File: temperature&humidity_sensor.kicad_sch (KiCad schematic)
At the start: 6 parts, among them U35 HDC1080

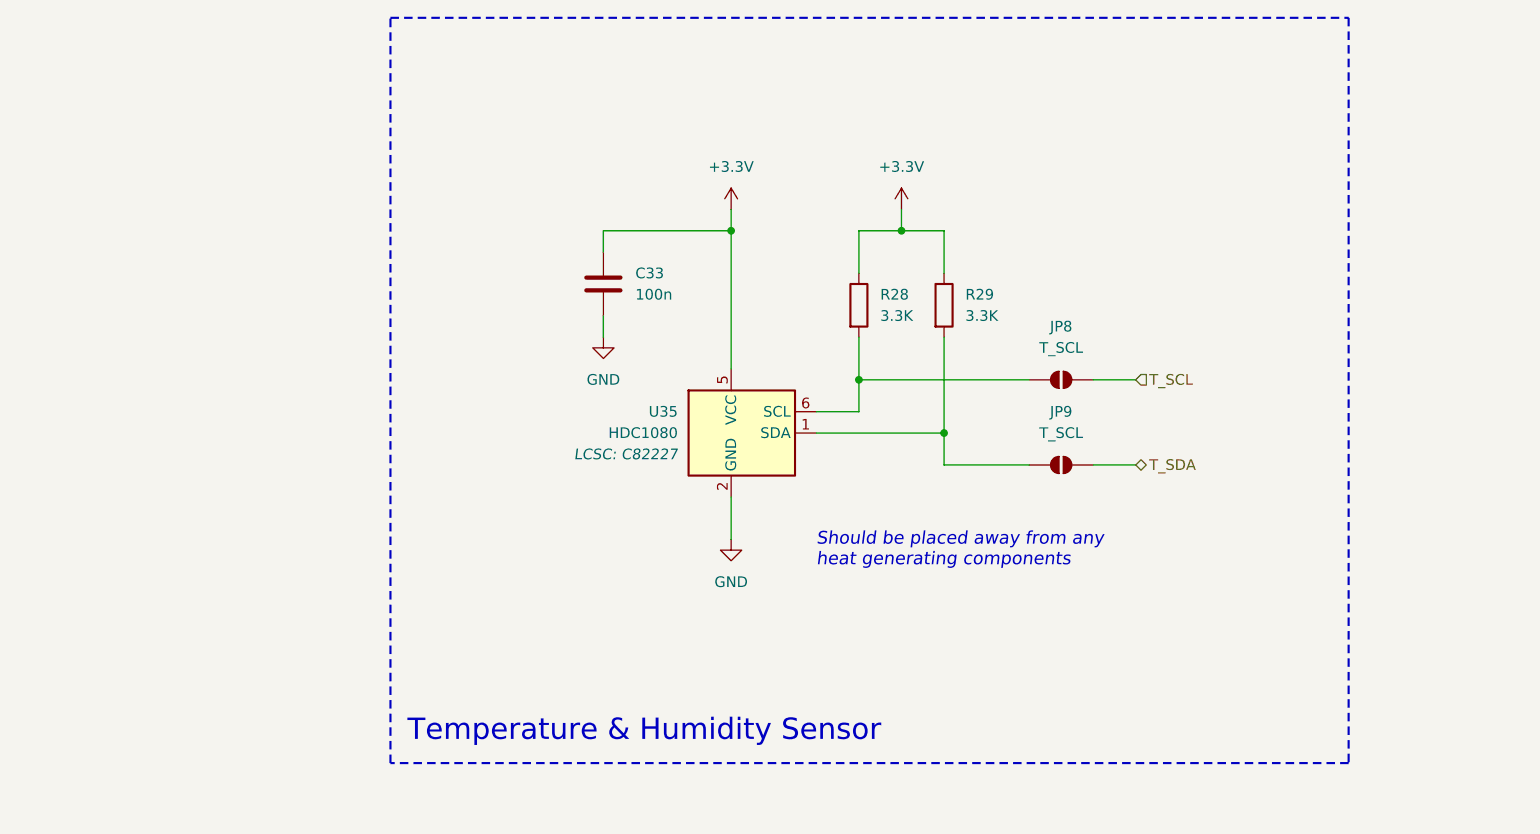
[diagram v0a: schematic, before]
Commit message: addition of bus
- cleaned up the structure of the schematic.
- addition of the colon
- root schematic improvements
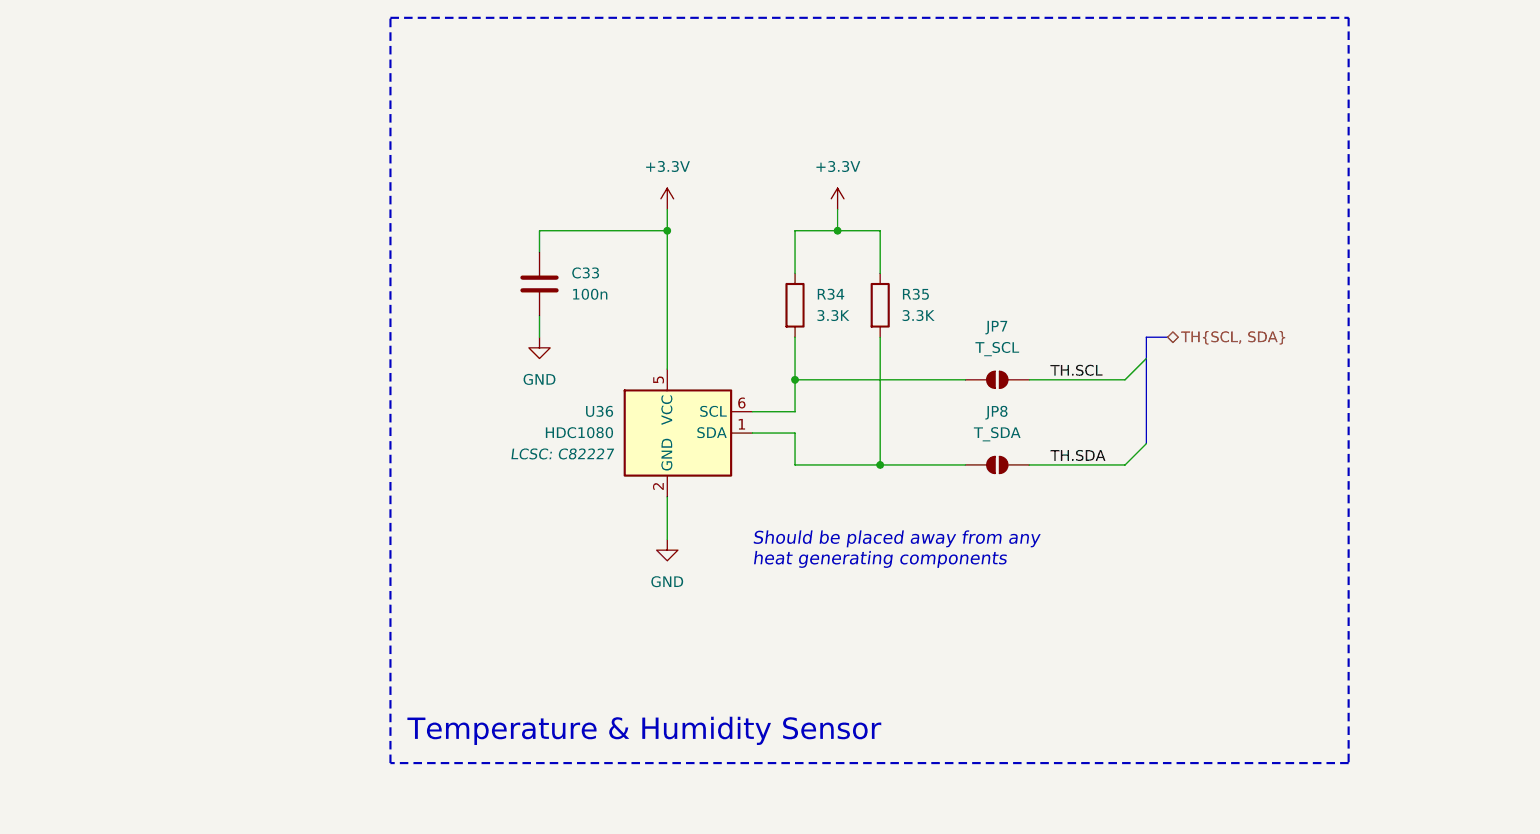
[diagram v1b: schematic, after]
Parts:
- JP8: renamed from JP9; value T_SCL -> T_SDA
- renumbered JP8 to JP7, R28 to R34, R29 to R35, U35 to U36
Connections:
- net T_SCL renamed TH.SCL
- net T_SDA renamed TH.SDA
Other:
- moved on the sheet: C33, JP7, JP8, R34, R35, U36

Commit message: current limiting resistor changes
- added colon led model, but might replace it in the future.
- reduction in current limiting resistance.
- removed the solder jumps in the individual circuit schematics.
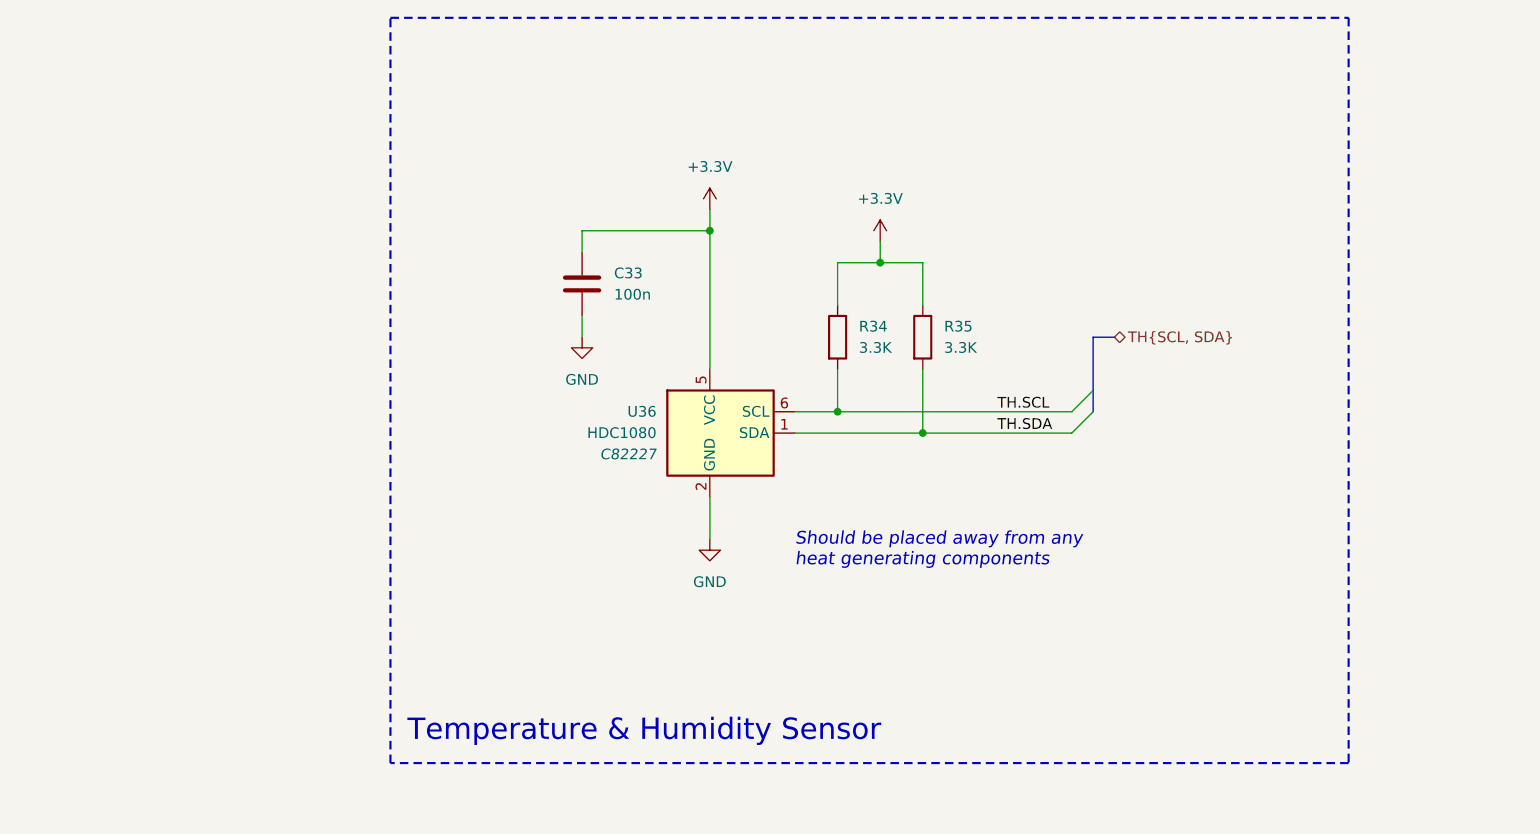
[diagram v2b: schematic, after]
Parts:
- removed JP7: T_SCL, Jumper:SolderJumper-2_P1.3mm_Open_TrianglePad1.0x1.5mm, symbol Jumper:SolderJumper_2_Open
- removed JP8: T_SDA, Jumper:SolderJumper-2_P1.3mm_Open_TrianglePad1.0x1.5mm, symbol Jumper:SolderJumper_2_Open
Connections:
- net TH.SCL: now also R34.2, U36.6 (SCL)
- net TH.SDA: now also R35.2, U36.1 (SDA)
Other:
- moved on the sheet: C33, R34, R35, U36

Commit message: voltage regulation changes
- ambient light sensor addition
- colon control
- brightness control through regulators
- added test points
- MCU pinout changes
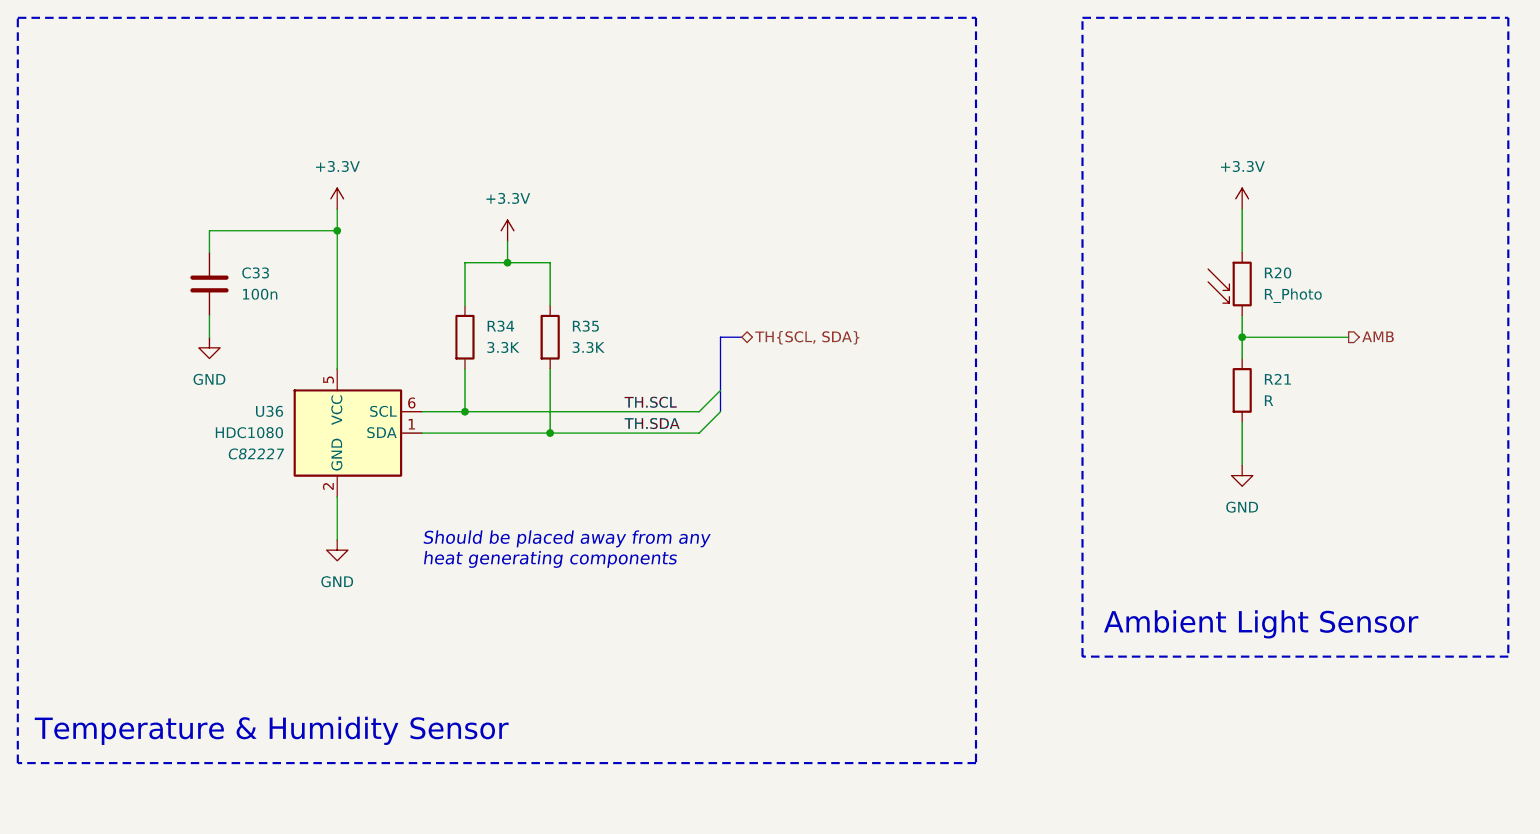
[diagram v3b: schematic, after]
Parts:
- added R20: R_Photo, symbol Device:R_Photo
- added R21: R, symbol Device:R
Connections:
- net +3.3V: now also R20.1
- net GND: now also R21.2
- new net AMB: R20.2, R21.1
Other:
- note added: "Ambient Light Sensor"
- moved on the sheet: C33, R34, R35, U36

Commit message: buzzer addition
- reordering
- test point addition
- ferrite beads on both the MCUs
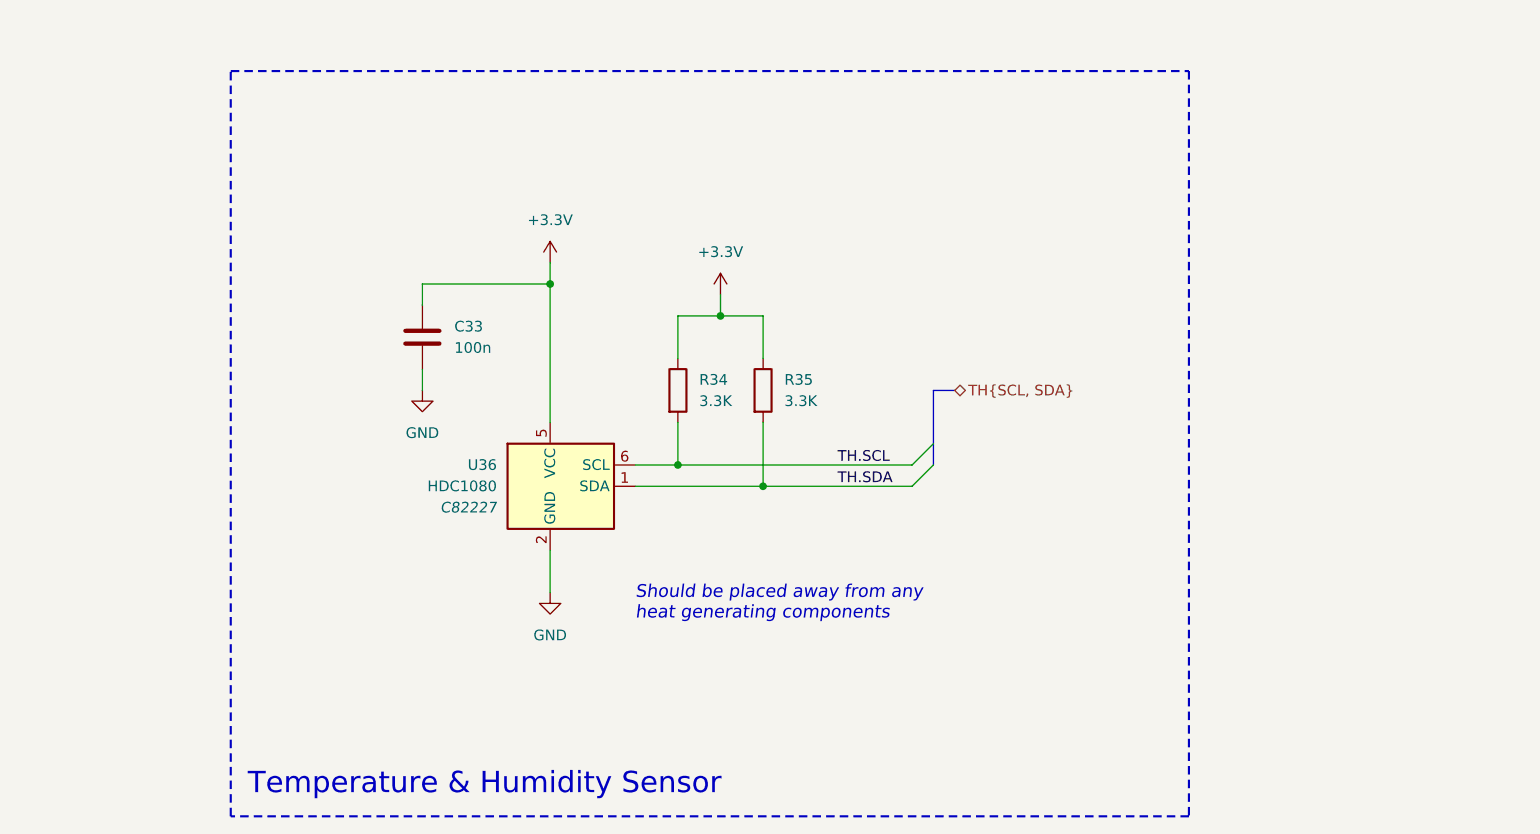
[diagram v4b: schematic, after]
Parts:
- removed R20: R_Photo, symbol Device:R_Photo
- removed R21: R, symbol Device:R
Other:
- note removed: "Ambient Light Sensor"
- moved on the sheet: C33, R34, R35, U36

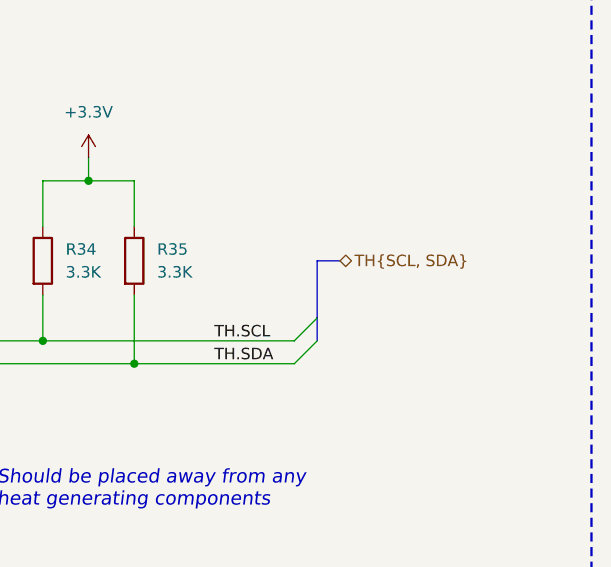
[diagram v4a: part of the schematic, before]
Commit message: Buzzer driver added - replacement of photoresistor to a variable resistor - added button - general formatting
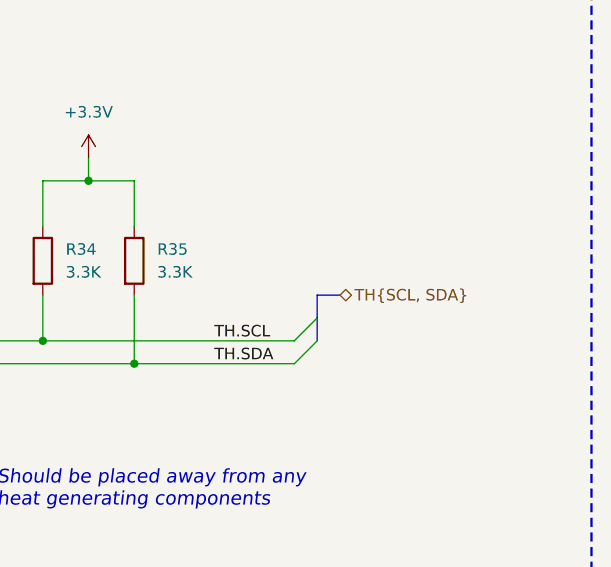
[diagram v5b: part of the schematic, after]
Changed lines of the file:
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@@
 	(bus
 		(pts
-			(xy 166.37 95.25) (xy 166.37 101.6)
+			(xy 166.37 99.06) (xy 166.37 101.6)
 		)
 		(stroke
@@
 	(bus
 		(pts
-			(xy 166.37 95.25) (xy 168.91 95.25)
+			(xy 166.37 99.06) (xy 168.91 99.06)
 		)
 		(stroke
@@
 	(hierarchical_label "TH{SCL, SDA}"
 		(shape bidirectional)
-		(at 168.91 95.25 0)
+		(at 168.91 99.06 0)
 		(effects
 			(font
